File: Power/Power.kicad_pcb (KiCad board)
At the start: 2 copper layers, 44 x 25 mm, 14 parts, among them J1 Conn_01x02, J2 Barrel_Jack, J3 Conn_01x02, J4 Conn_01x02, J5 Conn_01x02, J6 Conn_01x02, J7 Conn_01x02

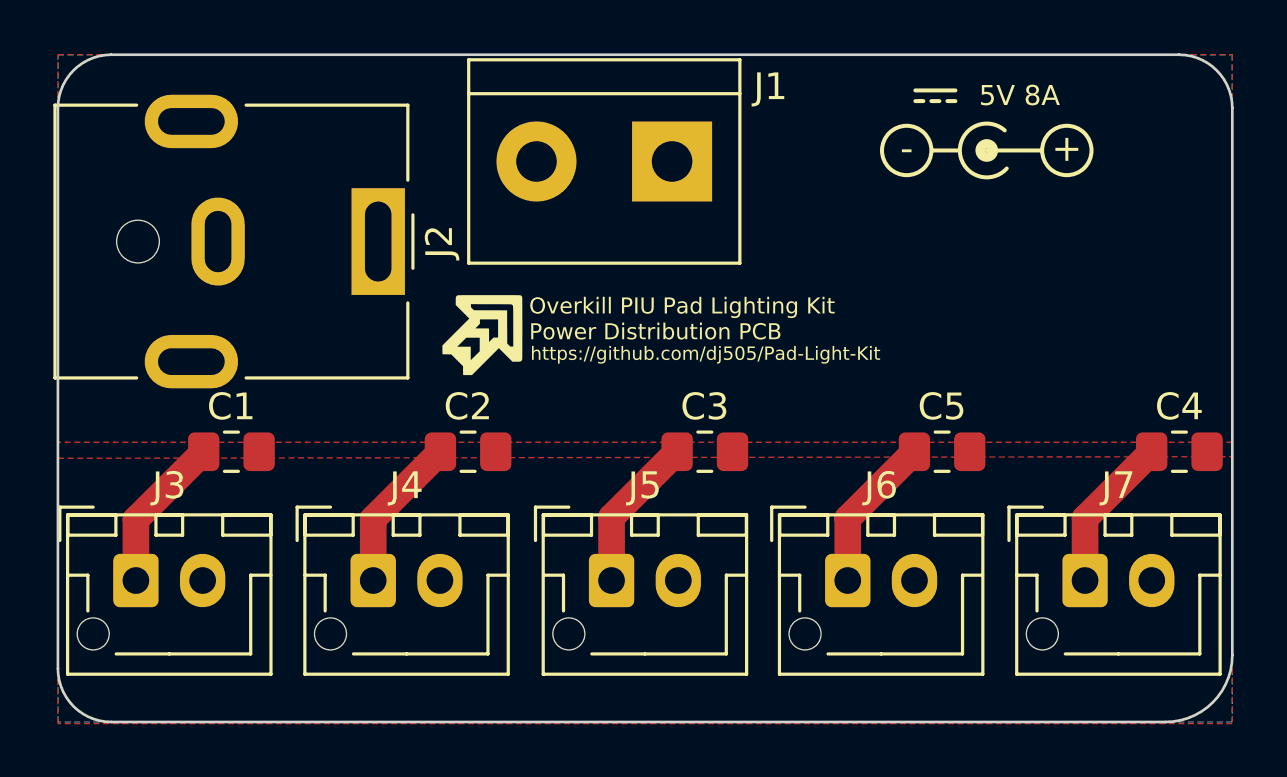
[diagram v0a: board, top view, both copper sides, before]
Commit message: Update power distribution PCB
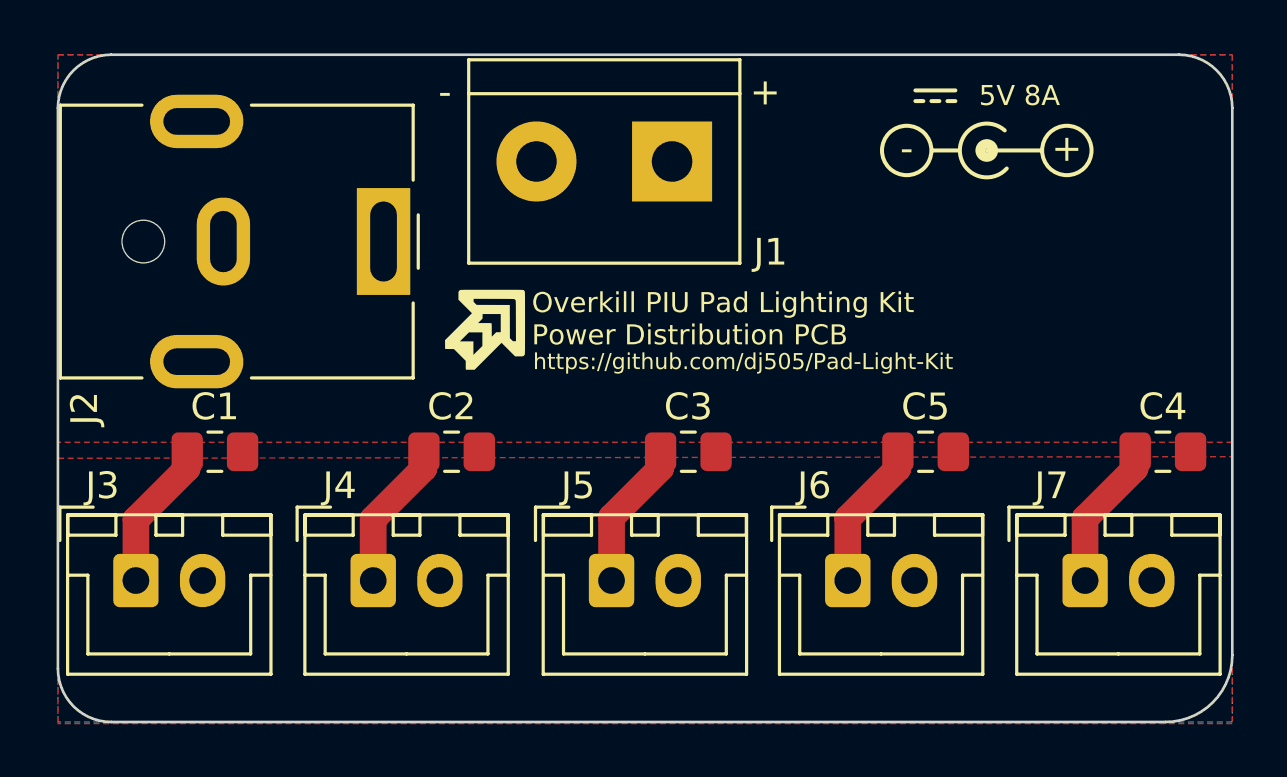
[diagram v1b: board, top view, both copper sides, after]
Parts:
- J3, J4, J5, J6, J7: footprint Connector_JST:JST_XH_B2B-XH-AM_1x02_P2.50mm_Vertical -> Connector_JST:JST_XH_B2B-XH-A_1x02_P2.50mm_Vertical
- moved C5 0.62 mm to (144.0, 98.9)
- moved C1 0.62 mm to (117.4, 98.9)
- moved C2 0.62 mm to (126.2, 98.9)
- moved C3 0.62 mm to (135.1, 98.9)
- moved C4 0.62 mm to (152.9, 98.9)
- moved G*** 0.22 mm to (127.5, 94.3)
- moved J2 0.20 mm to (123.7, 91.0)
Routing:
- net +5V: track 29.3 -> 28.0 mm
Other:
- board text added: "Attach with double sided adhesive"
